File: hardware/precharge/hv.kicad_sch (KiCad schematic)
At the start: 53 parts, among them Q1 BC856, Q2 BC856, Q3 BC856, U4 TLV274

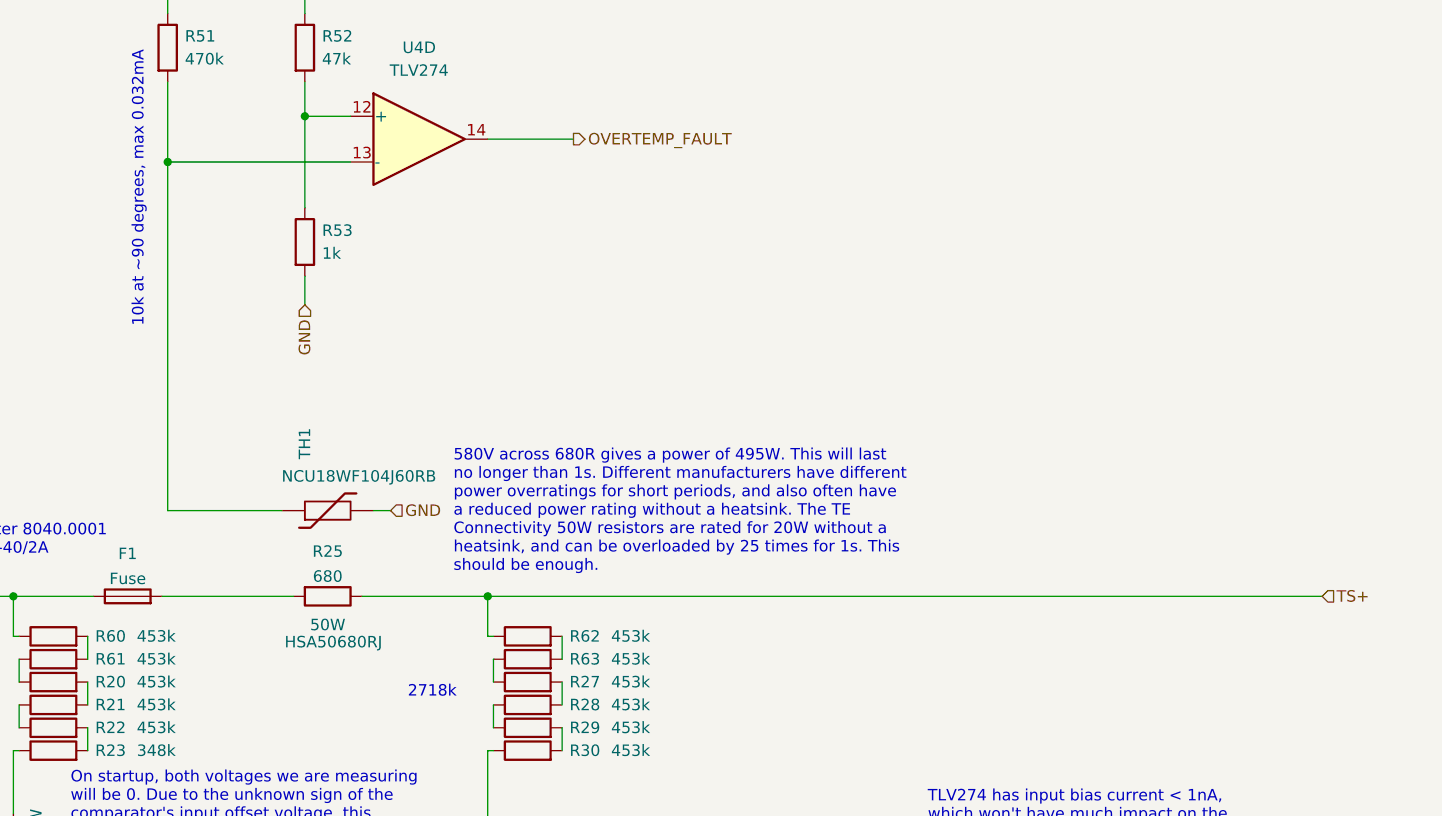
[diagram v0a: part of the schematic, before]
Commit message: Added precharge layout
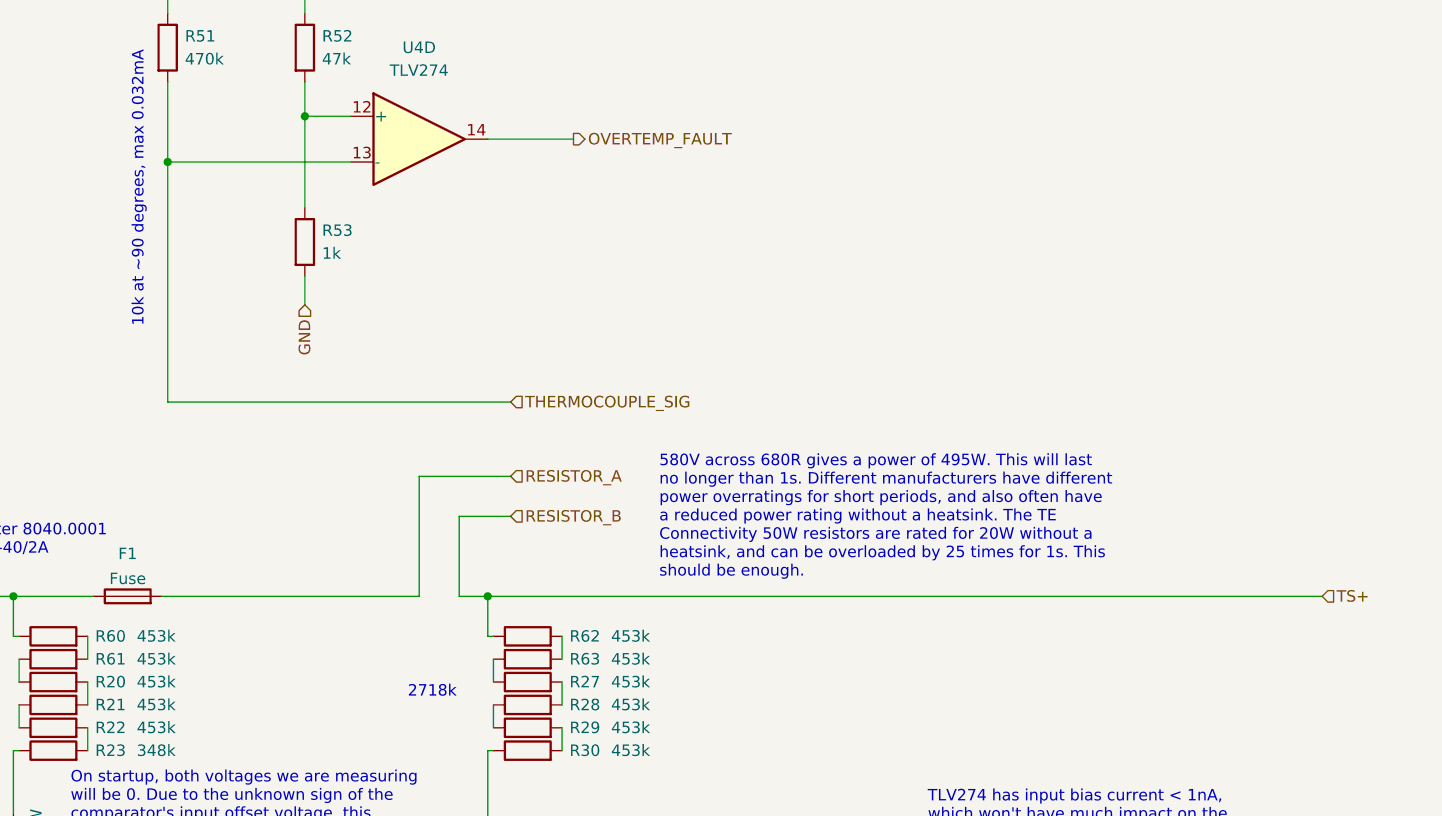
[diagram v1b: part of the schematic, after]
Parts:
- removed R25: 680, footprints:HSA50680RJ, symbol Device:R
- removed TH1: NCU18WF104J60RB, Resistor_SMD:R_0603_1608Metric, symbol Device:Thermistor
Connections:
- net RESISTOR_A: now reaches F1.2
- net THERMOCOUPLE_SIG: now reaches R51.2, U4.13 (-)
- net TS+ renamed RESISTOR_B
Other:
- title: (none) -> Precharge HV Side
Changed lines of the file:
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@@
 (kicad_sch (version 20211123) (generator eeschema)
   (paper "A3")
+  (title_block
+    (title "Precharge HV Side")
+  )
   (junction (at 266.065 146.05) (diameter 0) (color 0 0 0 0)
   )
@@
     (stroke (width 0) (type default) (color 0 0 0 0))
   )
-  (wire (pts (xy 175.895 90.805) (xy 188.595 90.805))
+  (wire (pts (xy 175.895 78.74) (xy 213.995 78.74))
     (stroke (width 0) (type default) (color 0 0 0 0))
   )
@@
     (stroke (width 0) (type default) (color 0 0 0 0))
   )
-  (wire (pts (xy 175.26 100.33) (xy 189.865 100.33))
+  (wire (pts (xy 175.26 100.33) (xy 203.835 100.33))
     (stroke (width 0) (type default) (color 0 0 0 0))
   )
@@
     (stroke (width 0) (type default) (color 0 0 0 0))
   )
-  (wire (pts (xy 175.895 52.07) (xy 175.895 90.805))
+  (wire (pts (xy 175.895 52.07) (xy 175.895 78.74))
     (stroke (width 0) (type default) (color 0 0 0 0))
   )
@@
     (stroke (width 0) (type default) (color 0 0 0 0))
   )
+  (wire (pts (xy 213.995 86.995) (xy 203.835 86.995))
+    (stroke (width 0) (type default) (color 0 0 0 0))
+  )
   (wire (pts (xy 158.75 100.33) (xy 158.75 104.775))
     (stroke (width 0) (type default) (color 0 0 0 0))
@@
     (stroke (width 0) (type default) (color 0 0 0 0))
   )
+  (wire (pts (xy 203.835 86.995) (xy 203.835 100.33))
+    (stroke (width 0) (type default) (color 0 0 0 0))
+  )
+  (wire (pts (xy 208.28 91.44) (xy 208.28 100.33))
+    (stroke (width 0) (type default) (color 0 0 0 0))
+  )
   (wire (pts (xy 113.665 145.415) (xy 113.03 145.415))
     (stroke (width 0) (type default) (color 0 0 0 0))
@@
     (stroke (width 0) (type default) (color 0 0 0 0))
   )
-  (wire (pts (xy 197.485 100.33) (xy 211.455 100.33))
-    (stroke (width 0) (type default) (color 0 0 0 0))
-  )
   (wire (pts (xy 175.895 179.705) (xy 175.895 183.515))
     (stroke (width 0) (type default) (color 0 0 0 0))
@@
     (stroke (width 0) (type default) (color 0 0 0 0))
   )
+  (wire (pts (xy 213.995 91.44) (xy 208.28 91.44))
+    (stroke (width 0) (type default) (color 0 0 0 0))
+  )
   (wire (pts (xy 211.455 140.97) (xy 211.455 186.69))
     (stroke (width 0) (type default) (color 0 0 0 0))
@@
     (stroke (width 0) (type default) (color 0 0 0 0))
   )
+  (wire (pts (xy 208.28 100.33) (xy 211.455 100.33))
+    (stroke (width 0) (type default) (color 0 0 0 0))
+  )
   (wire (pts (xy 123.19 132.715) (xy 123.19 135.255))
     (stroke (width 0) (type default) (color 0 0 0 0))
@@
   )
   (wire (pts (xy 183.515 184.785) (xy 183.515 195.58))
-    (stroke (width 0) (type default) (color 0 0 0 0))
-  )
-  (wire (pts (xy 198.755 90.805) (xy 200.66 90.805))
     (stroke (width 0) (type default) (color 0 0 0 0))
   )
@@
   )
   (text "580V across 680R gives a power of 495W. This will last\nno longer than 1s. Different manufacturers have different\npower overratings for short periods, and also often have\na reduced power rating without a heatsink. The TE\nConnectivity 50W resistors are rated for 20W without a\nheatsink, and can be overloaded by 25 times for 1s. This\nshould be enough."
-    (at 207.645 97.79 0)
+    (at 230.505 98.425 0)
     (effects (font (size 1.27 1.27)) (justify left bottom))
   )
@@
     (effects (font (size 1.27 1.27)) (justify right))
   )
+  (hierarchical_label "RESISTOR_B" (shape input) (at 213.995 91.44 0)
+    (effects (font (size 1.27 1.27)) (justify left))
+  )
+  (hierarchical_label "THERMOCOUPLE_SIG" (shape input) (at 213.995 78.74 0)
+    (effects (font (size 1.27 1.27)) (justify left))
+  )
   (hierarchical_label "+12V" (shape input) (at 173.99 236.22 90) (fields_autoplaced)
     (effects (font (size 1.27 1.27)) (justify left))
@@
     (effects (font (size 1.27 1.27)) (justify left))
   )
+  (hierarchical_label "RESISTOR_A" (shape input) (at 213.995 86.995 0)
+    (effects (font (size 1.27 1.27)) (justify left))
+  )
   (hierarchical_label "GND" (shape input) (at 191.135 67.945 270) (fields_autoplaced)
     (effects (font (size 1.27 1.27)) (justify right))
@@
     (effects (font (size 1.27 1.27)) (justify right))
   )
-  (hierarchical_label "GND" (shape input) (at 200.66 90.805 0) (fields_autoplaced)
-    (effects (font (size 1.27 1.27)) (justify left))
-  )
   (hierarchical_label "OVERTEMP_FAULT" (shape output) (at 220.98 49.53 0)
     (effects (font (size 1.27 1.27)) (justify left))
@@
       (effects (font (size 1.27 1.27)) hide)
     )
-    (pin "1")
-    (pin "2")
-  )
-  (symbol (lib_id "Device:R") (at 193.675 100.33 270) (unit 1)
-    (in_bom yes) (on_board yes)
-    (property "Reference" "R25" (id 0) (at 193.675 95.3475 90))
-    (property "Value" "680" (id 1) (at 193.675 98.1226 90))
-    (property "Footprint" "footprints:HSA50680RJ" (id 2) (at 193.675 98.552 90)
-      (effects (font (size 1.27 1.27)) hide)
-    )
-    (property "Datasheet" "~" (id 3) (at 193.675 100.33 0)
-      (effects (font (size 1.27 1.27)) hide)
-    )
-    (property "Power" "50W" (id 4) (at 193.675 103.505 90))
-    (property "MPN" "HSA50680RJ" (id 5) (at 194.31 105.41 90))
     (pin "1")
     (pin "2")
@@
       (effects (font (size 1.27 1.27)) hide)
     )
-    (pin "1")
-    (pin "2")
-  )
-  (symbol (lib_id "Device:Thermistor") (at 193.675 90.805 90) (unit 1)
-    (in_bom yes) (on_board yes)
-    (property "Reference" "TH1" (id 0) (at 191.135 85.09 0)
-      (effects (font (size 1.27 1.27)) (justify left))
-    )
-    (property "Value" "NCU18WF104J60RB" (id 1) (at 205.74 86.995 90)
-      (effects (font (size 1.27 1.27)) (justify left))
-    )
-    (property "Footprint" "Resistor_SMD:R_0603_1608Metric" (id 2) (at 193.675 90.805 0)
-      (effects (font (size 1.27 1.27)) hide)
-    )
-    (property "Datasheet" "~" (id 3) (at 193.675 90.805 0)
-      (effects (font (size 1.27 1.27)) hide)
-    )
